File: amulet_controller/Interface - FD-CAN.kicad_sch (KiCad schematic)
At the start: 4 parts, among them U12 TCAN1051HGVDRBRQ1

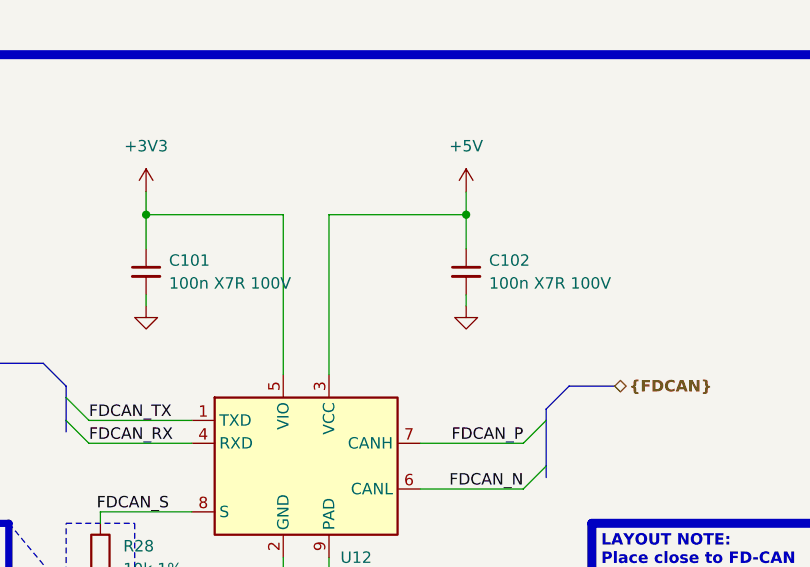
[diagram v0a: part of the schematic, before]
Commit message: filled in fields for bom, replaced inexisting components. Need to replace LEDs
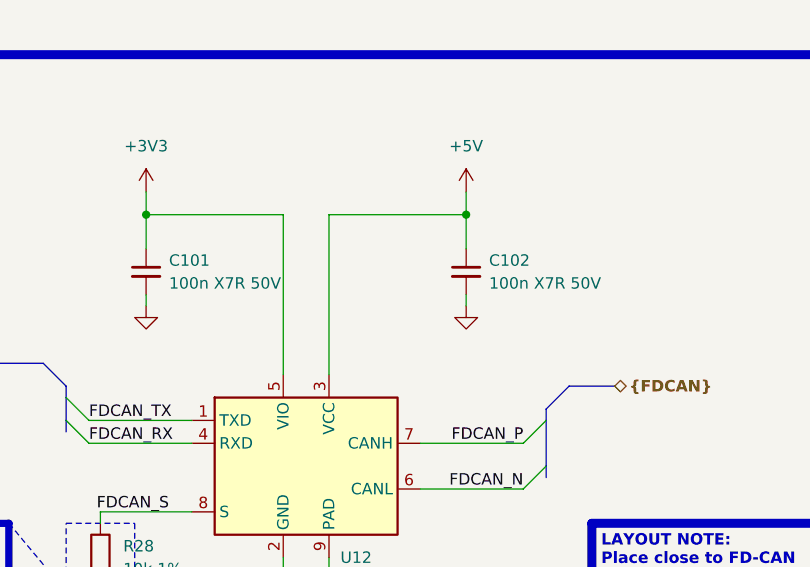
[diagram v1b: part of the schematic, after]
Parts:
- C101, C102: value 100n X7R 100V -> 100n X7R 50V; Manufacturer (none) -> Murata Electronics; Manufacturer Part Number (none) -> GCM155R71H104KE02J; Supplier 1 (none) -> Digikey; Supplier Part Number 1 (none) -> 490-14514-1-ND
- R28: Manufacturer (none) -> YAGEO; Manufacturer Part Number (none) -> RT0402FRE0710KL; Supplier 1 (none) -> Digikey; Supplier Part Number 1 (none) -> YAG1233CT-ND
- U12: Manufacturer (none) -> Texas Instruments; Manufacturer Part Number (none) -> TCAN1051HGVDRBRQ1; Supplier 1 (none) -> Digikey; Supplier Part Number 1 (none) -> 296-TCAN1051HGVDRBRQ1CT-ND
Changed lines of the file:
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@@
+      (effects (font (size 1.27 1.27)) hide)
+    )
+    (property "Description" "TCAN1051-Q1 Automotive Fault Protected CAN Transceiver with CAN FD" (at 152.4 95.25 0)
+      (effects (font (size 1.27 1.27)) hide)
+    )
+    (property "Manufacturer" "Texas Instruments" (at 152.4 95.25 0)
+      (effects (font (size 1.27 1.27)) hide)
+    )
+    (property "Manufacturer Part Number" "TCAN1051HGVDRBRQ1" (at 152.4 95.25 0)
+      (effects (font (size 1.27 1.27)) hide)
+    )
+    (property "Supplier 1" "Digikey" (at 152.4 95.25 0)
+      (effects (font (size 1.27 1.27)) hide)
+    )
+    (property "Supplier Part Number 1" "296-TCAN1051HGVDRBRQ1CT-ND" (at 152.4 95.25 0)
       (effects (font (size 1.27 1.27)) hide)
     )
@@
     (pin "9")
     (instances
-      (project "bldc_controller"
+      (project "amulet_controller"
         (path "/0650c7a8-acba-429c-9f8e-eec0baf0bc1c/fede4c36-00cc-4d3d-b71c-5243ba232202/95bf33d9-762c-4d08-af8b-3fad797ffaca"
           (reference "U12") (unit 1)
@@
     (pin "1")
     (instances
-      (project "bldc_controller"
+      (project "amulet_controller"
         (path "/0650c7a8-acba-429c-9f8e-eec0baf0bc1c/fede4c36-00cc-4d3d-b71c-5243ba232202/95bf33d9-762c-4d08-af8b-3fad797ffaca"
           (reference "#PWR054") (unit 1)
@@
     (pin "1")
     (instances
-      (project "bldc_controller"
+      (project "amulet_controller"
         (path "/0650c7a8-acba-429c-9f8e-eec0baf0bc1c/fede4c36-00cc-4d3d-b71c-5243ba232202/95bf33d9-762c-4d08-af8b-3fad797ffaca"
           (reference "#PWR053") (unit 1)
@@
     (pin "1")
     (instances
-      (project "bldc_controller"
+      (project "amulet_controller"
         (path "/0650c7a8-acba-429c-9f8e-eec0baf0bc1c/fede4c36-00cc-4d3d-b71c-5243ba232202/95bf33d9-762c-4d08-af8b-3fad797ffaca"
           (reference "#PWR055") (unit 1)
@@
     (pin "1")
     (instances
-      (project "bldc_controller"
+      (project "amulet_controller"
         (path "/0650c7a8-acba-429c-9f8e-eec0baf0bc1c/fede4c36-00cc-4d3d-b71c-5243ba232202/95bf33d9-762c-4d08-af8b-3fad797ffaca"
           (reference "#PWR057") (unit 1)
@@
       (effects (font (size 1.27 1.27)) (justify left))
     )
-    (property "Value" "100n X7R 100V" (at 172.72 74.9363 0)
+    (property "Value" "100n X7R 50V" (at 172.72 74.9363 0)
       (effects (font (size 1.27 1.27)) (justify left))
     )
@@
       (effects (font (size 1.27 1.27)) hide)
     )
-    (property "Datasheet" "~" (at 170.18 73.66 0)
-      (effects (font (size 1.27 1.27)) hide)
-    )
-    (pin "1")
-    (pin "2")
-    (instances
-      (project "bldc_controller"
+    (property "Datasheet" "https://search.murata.co.jp/Ceramy/image/img/A01X/G101/ENG/GCM155R71H104KE02-01.pdf" (at 170.18 73.66 0)
+      (effects (font (size 1.27 1.27)) hide)
+    )
+    (property "Description" "0.1 µF ±10% 50V Ceramic Capacitor X7R 0402 (1005 Metric)" (at 170.18 73.66 0)
+      (effects (font (size 1.27 1.27)) hide)
+    )
+    (property "Manufacturer" "Murata Electronics" (at 170.18 73.66 0)
+      (effects (font (size 1.27 1.27)) hide)
+    )
+    (property "Manufacturer Part Number" "GCM155R71H104KE02J" (at 170.18 73.66 0)
+      (effects (font (size 1.27 1.27)) hide)
+    )
+    (property "Supplier 1" "Digikey" (at 170.18 73.66 0)
+      (effects (font (size 1.27 1.27)) hide)
+    )
+    (property "Supplier Part Number 1" "490-14514-1-ND" (at 170.18 73.66 0)
+      (effects (font (size 1.27 1.27)) hide)
+    )
+    (pin "1")
+    (pin "2")
+    (instances
+      (project "amulet_controller"
         (path "/0650c7a8-acba-429c-9f8e-eec0baf0bc1c/fede4c36-00cc-4d3d-b71c-5243ba232202/95bf33d9-762c-4d08-af8b-3fad797ffaca"
           (reference "C102") (unit 1)
@@
     (pin "1")
     (instances
-      (project "bldc_controller"
+      (project "amulet_controller"
         (path "/0650c7a8-acba-429c-9f8e-eec0baf0bc1c/fede4c36-00cc-4d3d-b71c-5243ba232202/95bf33d9-762c-4d08-af8b-3fad797ffaca"
           (reference "#PWR056") (unit 1)
@@
       (effects (font (size 1.27 1.27)) (justify left))
     )
-    (property "Value" "100n X7R 100V" (at 137.16 74.9363 0)
+    (property "Value" "100n X7R 50V" (at 137.16 74.9363 0)
       (effects (font (size 1.27 1.27)) (justify left))
     )
@@
       (effects (font (size 1.27 1.27)) hide)
     )
-    (property "Datasheet" "~" (at 134.62 73.66 0)
-      (effects (font (size 1.27 1.27)) hide)
-    )
-    (pin "1")
-    (pin "2")
-    (instances
-      (project "bldc_controller"
+    (property "Datasheet" "https://search.murata.co.jp/Ceramy/image/img/A01X/G101/ENG/GCM155R71H104KE02-01.pdf" (at 134.62 73.66 0)
+      (effects (font (size 1.27 1.27)) hide)
+    )
+    (property "Description" "0.1 µF ±10% 50V Ceramic Capacitor X7R 0402 (1005 Metric)" (at 134.62 73.66 0)
+      (effects (font (size 1.27 1.27)) hide)
+    )
+    (property "Manufacturer" "Murata Electronics" (at 134.62 73.66 0)
+      (effects (font (size 1.27 1.27)) hide)
+    )
+    (property "Manufacturer Part Number" "GCM155R71H104KE02J" (at 134.62 73.66 0)
+      (effects (font (size 1.27 1.27)) hide)
+    )
+    (property "Supplier 1" "Digikey" (at 134.62 73.66 0)
+      (effects (font (size 1.27 1.27)) hide)
+    )
+    (property "Supplier Part Number 1" "490-14514-1-ND" (at 134.62 73.66 0)
+      (effects (font (size 1.27 1.27)) hide)
+    )
+    (pin "1")
+    (pin "2")
+    (instances
+      (project "amulet_controller"
         (path "/0650c7a8-acba-429c-9f8e-eec0baf0bc1c/fede4c36-00cc-4d3d-b71c-5243ba232202/95bf33d9-762c-4d08-af8b-3fad797ffaca"
           (reference "C101") (unit 1)
@@
       (effects (font (size 1.27 1.27)) hide)
     )
-    (property "Datasheet" "~" (at 129.54 105.41 0)
-      (effects (font (size 1.27 1.27)) hide)
-    )
-    (pin "1")
-    (pin "2")
-    (instances
-      (project "bldc_controller"
+    (property "Datasheet" "https://www.yageo.com/upload/media/product/app/datasheet/rchip/pyu-rt_1-to-0.01_rohs_l.pdf" (at 129.54 105.41 0)
+      (effects (font (size 1.27 1.27)) hide)
+    )
+    (property "Description" "RES SMD 10K OHM 1% 1/16W 0402 50PPM" (at 129.54 105.41 0)
+      (effects (font (size 1.27 1.27)) hide)
+    )
+    (property "Manufacturer" "YAGEO" (at 129.54 105.41 0)
+      (effects (font (size 1.27 1.27)) hide)
+    )
+    (property "Manufacturer Part Number" "RT0402FRE0710KL" (at 129.54 105.41 0)
+      (effects (font (size 1.27 1.27)) hide)
+    )
+    (property "Supplier 1" "Digikey" (at 129.54 105.41 0)
+      (effects (font (size 1.27 1.27)) hide)
+    )
+    (property "Supplier Part Number 1" "YAG1233CT-ND" (at 129.54 105.41 0)
+      (effects (font (size 1.27 1.27)) hide)
+    )
+    (pin "1")
+    (pin "2")
+    (instances
+      (project "amulet_controller"
         (path "/0650c7a8-acba-429c-9f8e-eec0baf0bc1c/fede4c36-00cc-4d3d-b71c-5243ba232202/95bf33d9-762c-4d08-af8b-3fad797ffaca"
           (reference "R28") (unit 1)

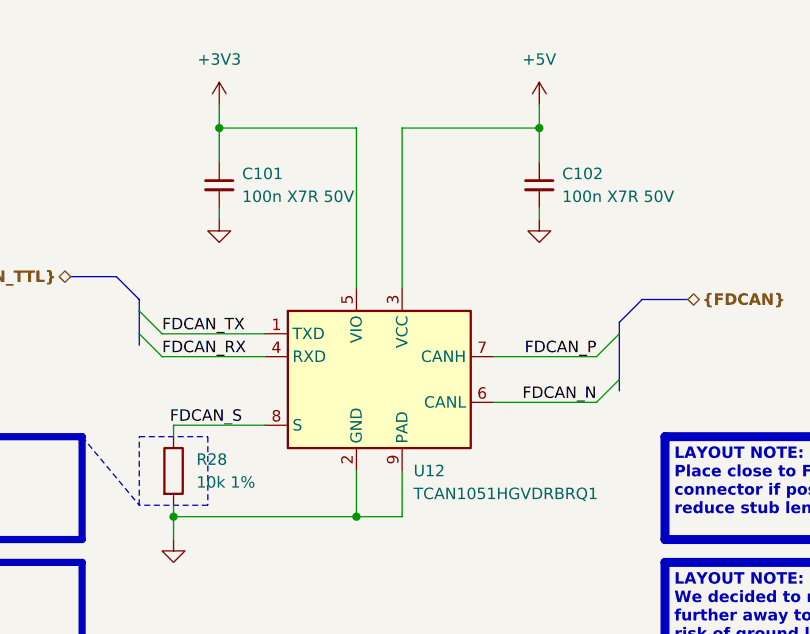
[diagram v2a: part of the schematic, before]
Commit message: finalized pcb. TODO: add clean BOM and KiBot integration
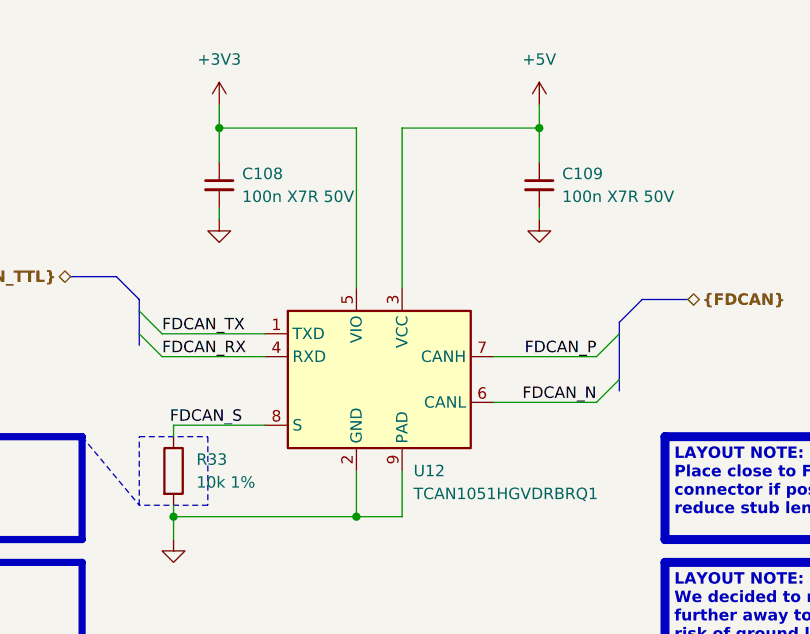
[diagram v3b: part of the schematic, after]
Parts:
- renumbered C101 to C108, C102 to C109, R28 to R33
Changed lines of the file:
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@@
   (symbol (lib_id "power:+3V3") (at 134.62 64.77 0) (unit 1)
     (in_bom yes) (on_board yes) (dnp no) (fields_autoplaced)
-    (property "Reference" "#PWR054" (at 134.62 68.58 0)
+    (property "Reference" "#PWR055" (at 134.62 68.58 0)
       (effects (font (size 1.27 1.27)) hide)
     )
@@
       (project "amulet_controller"
         (path "/0650c7a8-acba-429c-9f8e-eec0baf0bc1c/fede4c36-00cc-4d3d-b71c-5243ba232202/95bf33d9-762c-4d08-af8b-3fad797ffaca"
+          (reference "#PWR055") (unit 1)
+        )
+      )
+    )
+  )
+  (symbol (lib_id "power:GND") (at 129.54 113.03 0) (unit 1)
+    (in_bom yes) (on_board yes) (dnp no) (fields_autoplaced)
+    (property "Reference" "#PWR054" (at 129.54 119.38 0)
+      (effects (font (size 1.27 1.27)) hide)
+    )
+    (property "Value" "GND" (at 129.54 118.11 0)
+      (effects (font (size 1.27 1.27)) hide)
+    )
+    (property "Footprint" "" (at 129.54 113.03 0)
+      (effects (font (size 1.27 1.27)) hide)
+    )
+    (property "Datasheet" "" (at 129.54 113.03 0)
+      (effects (font (size 1.27 1.27)) hide)
+    )
+    (pin "1")
+    (instances
+      (project "amulet_controller"
+        (path "/0650c7a8-acba-429c-9f8e-eec0baf0bc1c/fede4c36-00cc-4d3d-b71c-5243ba232202/95bf33d9-762c-4d08-af8b-3fad797ffaca"
           (reference "#PWR054") (unit 1)
-        )
-      )
-    )
-  )
-  (symbol (lib_id "power:GND") (at 129.54 113.03 0) (unit 1)
-    (in_bom yes) (on_board yes) (dnp no) (fields_autoplaced)
-    (property "Reference" "#PWR053" (at 129.54 119.38 0)
-      (effects (font (size 1.27 1.27)) hide)
-    )
-    (property "Value" "GND" (at 129.54 118.11 0)
-      (effects (font (size 1.27 1.27)) hide)
-    )
-    (property "Footprint" "" (at 129.54 113.03 0)
-      (effects (font (size 1.27 1.27)) hide)
-    )
-    (property "Datasheet" "" (at 129.54 113.03 0)
-      (effects (font (size 1.27 1.27)) hide)
-    )
-    (pin "1")
-    (instances
-      (project "amulet_controller"
-        (path "/0650c7a8-acba-429c-9f8e-eec0baf0bc1c/fede4c36-00cc-4d3d-b71c-5243ba232202/95bf33d9-762c-4d08-af8b-3fad797ffaca"
-          (reference "#PWR053") (unit 1)
         )
       )
@@
   (symbol (lib_id "power:GND") (at 134.62 77.47 0) (unit 1)
     (in_bom yes) (on_board yes) (dnp no)
-    (property "Reference" "#PWR055" (at 134.62 83.82 0)
+    (property "Reference" "#PWR056" (at 134.62 83.82 0)
       (effects (font (size 1.27 1.27)) hide)
     )
@@
       (project "amulet_controller"
         (path "/0650c7a8-acba-429c-9f8e-eec0baf0bc1c/fede4c36-00cc-4d3d-b71c-5243ba232202/95bf33d9-762c-4d08-af8b-3fad797ffaca"
-          (reference "#PWR055") (unit 1)
+          (reference "#PWR056") (unit 1)
         )
       )
@@
   (symbol (lib_id "power:GND") (at 170.18 77.47 0) (mirror y) (unit 1)
     (in_bom yes) (on_board yes) (dnp no) (fields_autoplaced)
-    (property "Reference" "#PWR057" (at 170.18 83.82 0)
+    (property "Reference" "#PWR058" (at 170.18 83.82 0)
       (effects (font (size 1.27 1.27)) hide)
     )
@@
       (project "amulet_controller"
         (path "/0650c7a8-acba-429c-9f8e-eec0baf0bc1c/fede4c36-00cc-4d3d-b71c-5243ba232202/95bf33d9-762c-4d08-af8b-3fad797ffaca"
-          (reference "#PWR057") (unit 1)
+          (reference "#PWR058") (unit 1)
         )
       )
@@
   (symbol (lib_id "Device:C_Small") (at 170.18 73.66 0) (unit 1)
     (in_bom yes) (on_board yes) (dnp no)
-    (property "Reference" "C102" (at 172.72 72.3963 0)
+    (property "Reference" "C109" (at 172.72 72.3963 0)
       (effects (font (size 1.27 1.27)) (justify left))
     )
@@
       (project "amulet_controller"
         (path "/0650c7a8-acba-429c-9f8e-eec0baf0bc1c/fede4c36-00cc-4d3d-b71c-5243ba232202/95bf33d9-762c-4d08-af8b-3fad797ffaca"
-          (reference "C102") (unit 1)
+          (reference "C109") (unit 1)
         )
       )
@@
   (symbol (lib_id "power:+5V") (at 170.18 64.77 0) (unit 1)
     (in_bom yes) (on_board yes) (dnp no) (fields_autoplaced)
-    (property "Reference" "#PWR056" (at 170.18 68.58 0)
+    (property "Reference" "#PWR057" (at 170.18 68.58 0)
       (effects (font (size 1.27 1.27)) hide)
     )
@@
       (project "amulet_controller"
         (path "/0650c7a8-acba-429c-9f8e-eec0baf0bc1c/fede4c36-00cc-4d3d-b71c-5243ba232202/95bf33d9-762c-4d08-af8b-3fad797ffaca"
-          (reference "#PWR056") (unit 1)
+          (reference "#PWR057") (unit 1)
         )
       )
@@
   (symbol (lib_id "Device:C_Small") (at 134.62 73.66 0) (unit 1)
     (in_bom yes) (on_board yes) (dnp no) (fields_autoplaced)
-    (property "Reference" "C101" (at 137.16 72.3963 0)
+    (property "Reference" "C108" (at 137.16 72.3963 0)
       (effects (font (size 1.27 1.27)) (justify left))
     )
@@
       (project "amulet_controller"
         (path "/0650c7a8-acba-429c-9f8e-eec0baf0bc1c/fede4c36-00cc-4d3d-b71c-5243ba232202/95bf33d9-762c-4d08-af8b-3fad797ffaca"
-          (reference "C101") (unit 1)
+          (reference "C108") (unit 1)
         )
       )
@@
   (symbol (lib_id "Device:R") (at 129.54 105.41 0) (unit 1)
     (in_bom yes) (on_board yes) (dnp no) (fields_autoplaced)
-    (property "Reference" "R28" (at 132.08 104.14 0)
+    (property "Reference" "R33" (at 132.08 104.14 0)
       (effects (font (size 1.27 1.27)) (justify left))
     )
@@
       (project "amulet_controller"
         (path "/0650c7a8-acba-429c-9f8e-eec0baf0bc1c/fede4c36-00cc-4d3d-b71c-5243ba232202/95bf33d9-762c-4d08-af8b-3fad797ffaca"
-          (reference "R28") (unit 1)
-        )
-      )
+          (reference "R33") (unit 1)
+        )
+      )

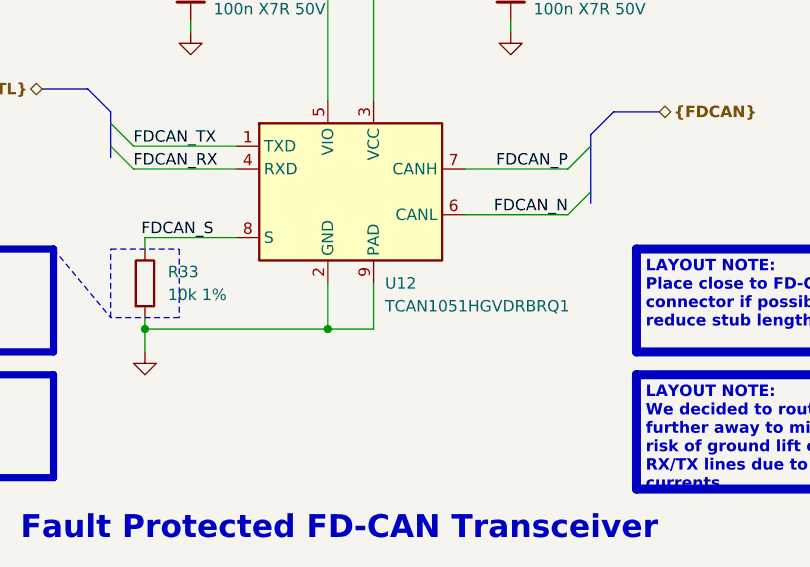
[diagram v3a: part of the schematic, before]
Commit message: corrected pcb according to reviews on reddit
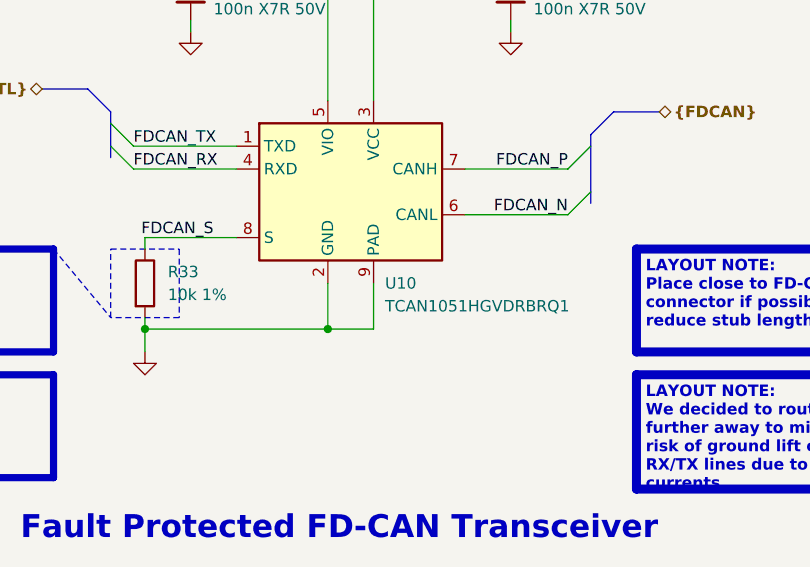
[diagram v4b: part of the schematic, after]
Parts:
- renumbered U12 to U10
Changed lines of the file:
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@@
   (symbol (lib_id "0_interface_can:TCAN1051HGVDRBRQ1") (at 152.4 95.25 0) (unit 1)
     (in_bom yes) (on_board yes) (dnp no)
-    (property "Reference" "U12" (at 156.21 105.41 0)
+    (property "Reference" "U10" (at 156.21 105.41 0)
       (effects (font (size 1.27 1.27)) (justify left))
     )
@@
       (project "amulet_controller"
         (path "/0650c7a8-acba-429c-9f8e-eec0baf0bc1c/fede4c36-00cc-4d3d-b71c-5243ba232202/95bf33d9-762c-4d08-af8b-3fad797ffaca"
-          (reference "U12") (unit 1)
+          (reference "U10") (unit 1)
         )
       )
@@
   (symbol (lib_id "power:+3V3") (at 134.62 64.77 0) (unit 1)
     (in_bom yes) (on_board yes) (dnp no) (fields_autoplaced)
-    (property "Reference" "#PWR055" (at 134.62 68.58 0)
+    (property "Reference" "#PWR056" (at 134.62 68.58 0)
       (effects (font (size 1.27 1.27)) hide)
     )
@@
       (project "amulet_controller"
         (path "/0650c7a8-acba-429c-9f8e-eec0baf0bc1c/fede4c36-00cc-4d3d-b71c-5243ba232202/95bf33d9-762c-4d08-af8b-3fad797ffaca"
-          (reference "#PWR055") (unit 1)
+          (reference "#PWR056") (unit 1)
         )
       )
@@
   (symbol (lib_id "power:GND") (at 129.54 113.03 0) (unit 1)
     (in_bom yes) (on_board yes) (dnp no) (fields_autoplaced)
-    (property "Reference" "#PWR054" (at 129.54 119.38 0)
+    (property "Reference" "#PWR055" (at 129.54 119.38 0)
       (effects (font (size 1.27 1.27)) hide)
     )
@@
       (project "amulet_controller"
         (path "/0650c7a8-acba-429c-9f8e-eec0baf0bc1c/fede4c36-00cc-4d3d-b71c-5243ba232202/95bf33d9-762c-4d08-af8b-3fad797ffaca"
-          (reference "#PWR054") (unit 1)
+          (reference "#PWR055") (unit 1)
         )
       )
@@
   (symbol (lib_id "power:GND") (at 134.62 77.47 0) (unit 1)
     (in_bom yes) (on_board yes) (dnp no)
-    (property "Reference" "#PWR056" (at 134.62 83.82 0)
+    (property "Reference" "#PWR057" (at 134.62 83.82 0)
       (effects (font (size 1.27 1.27)) hide)
     )
@@
       (project "amulet_controller"
         (path "/0650c7a8-acba-429c-9f8e-eec0baf0bc1c/fede4c36-00cc-4d3d-b71c-5243ba232202/95bf33d9-762c-4d08-af8b-3fad797ffaca"
-          (reference "#PWR056") (unit 1)
+          (reference "#PWR057") (unit 1)
         )
       )
@@
   (symbol (lib_id "power:GND") (at 170.18 77.47 0) (mirror y) (unit 1)
     (in_bom yes) (on_board yes) (dnp no) (fields_autoplaced)
-    (property "Reference" "#PWR058" (at 170.18 83.82 0)
+    (property "Reference" "#PWR059" (at 170.18 83.82 0)
       (effects (font (size 1.27 1.27)) hide)
     )
@@
       (project "amulet_controller"
         (path "/0650c7a8-acba-429c-9f8e-eec0baf0bc1c/fede4c36-00cc-4d3d-b71c-5243ba232202/95bf33d9-762c-4d08-af8b-3fad797ffaca"
-          (reference "#PWR058") (unit 1)
+          (reference "#PWR059") (unit 1)
         )
       )
@@
   (symbol (lib_id "power:+5V") (at 170.18 64.77 0) (unit 1)
     (in_bom yes) (on_board yes) (dnp no) (fields_autoplaced)
-    (property "Reference" "#PWR057" (at 170.18 68.58 0)
+    (property "Reference" "#PWR058" (at 170.18 68.58 0)
       (effects (font (size 1.27 1.27)) hide)
     )
@@
       (project "amulet_controller"
         (path "/0650c7a8-acba-429c-9f8e-eec0baf0bc1c/fede4c36-00cc-4d3d-b71c-5243ba232202/95bf33d9-762c-4d08-af8b-3fad797ffaca"
-          (reference "#PWR057") (unit 1)
+          (reference "#PWR058") (unit 1)
         )
       )
